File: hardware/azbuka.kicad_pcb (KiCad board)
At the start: 2 copper layers, 10 parts, among them IC1 ATTINY85-S, P1 USB_OTG, P2 CONN_01X06, Q1 MOSFET_P_CH, U1 AP111733, U2 TXS0102, U3 SJ1-3524NG

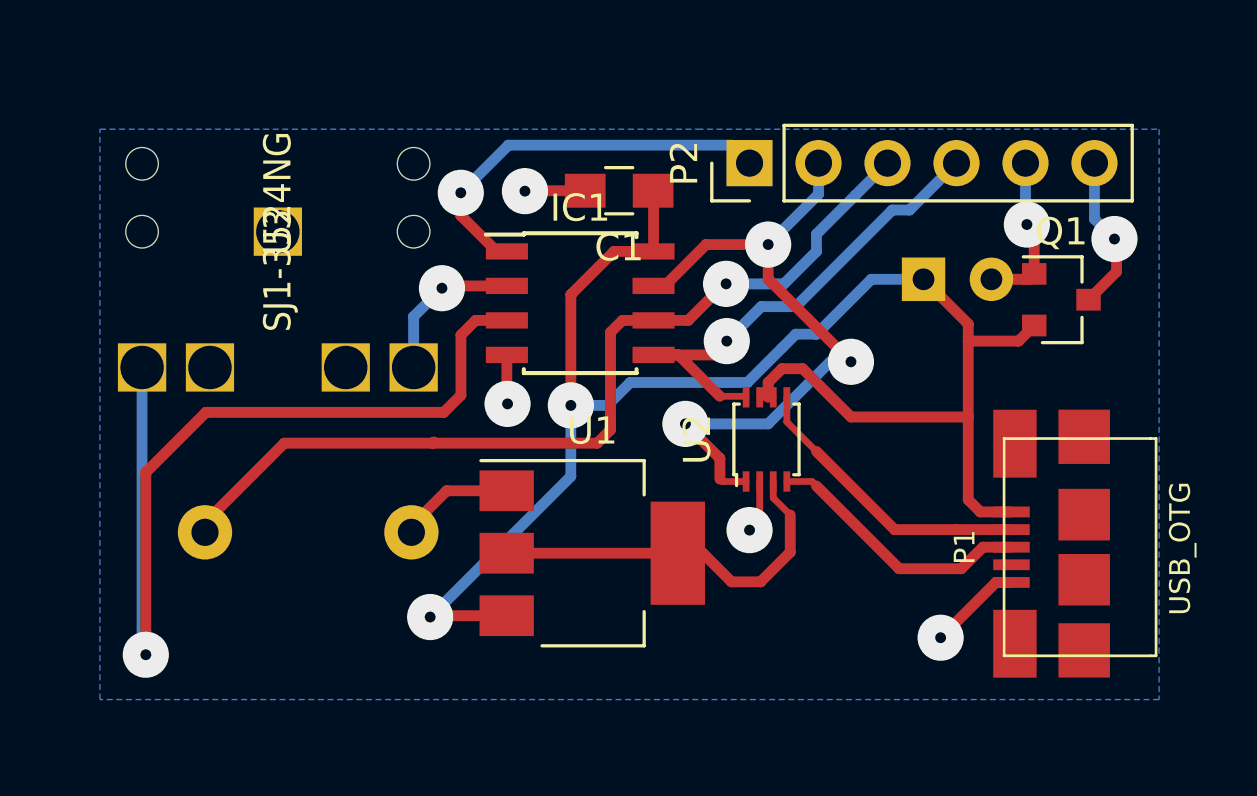
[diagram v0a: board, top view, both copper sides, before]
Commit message: Updating board file to include USB's required series resistors, 1.5k pullup; fixed ATTINY85 footprint; minor layout changes.
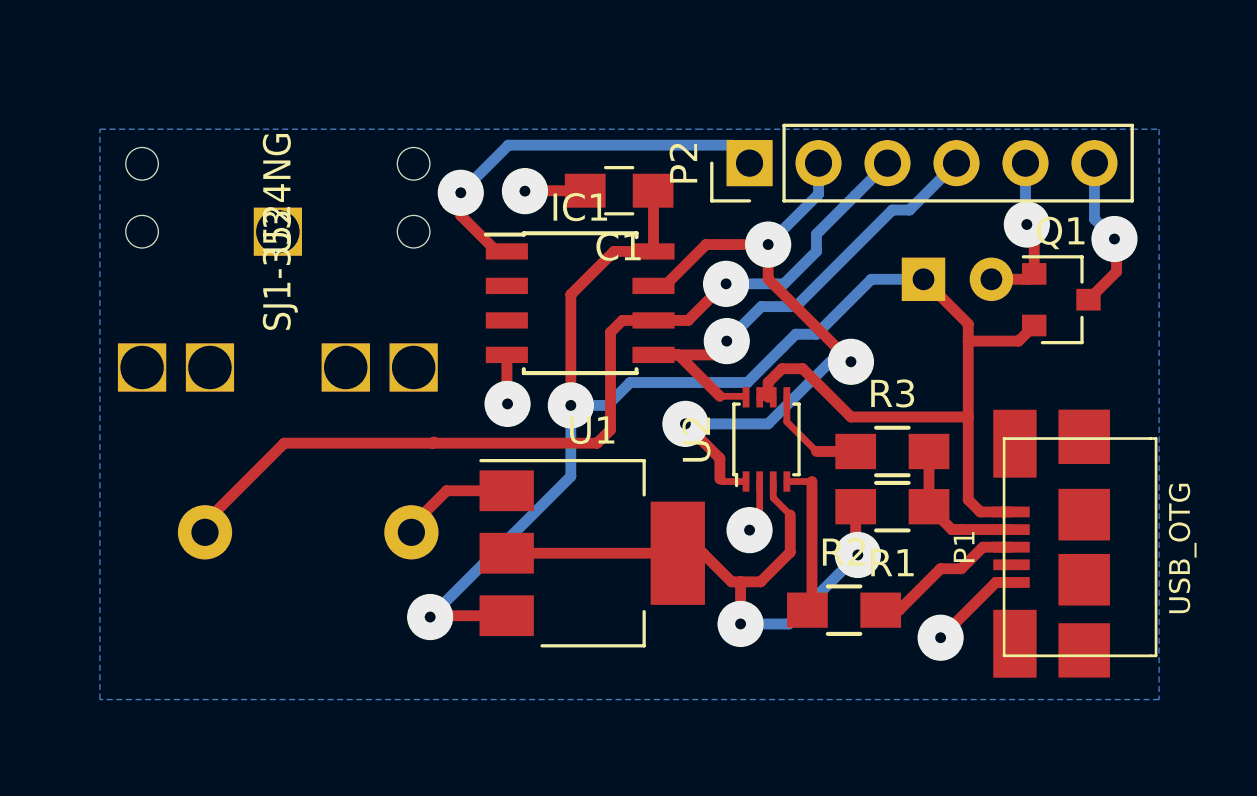
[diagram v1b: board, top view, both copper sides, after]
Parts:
- added R1: 1.5k, Resistors_SMD:R_0805_HandSoldering, F.Cu at (154.2, 72.9)
- added R2: 47, Resistors_SMD:R_0805_HandSoldering, F.Cu at (152.4, 76.7)
- added R3: 47, Resistors_SMD:R_0805_HandSoldering, F.Cu at (154.2, 70.9)
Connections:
- U2 pad 4: Net-(P1-Pad3) -> Net-(R2-Pad1)
- U2 pad 5: Net-(P1-Pad2) -> Net-(R3-Pad1)
- U3 pad 2: DAH -> DIT
- U3 pad 3: DIT -> DAH
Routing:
- net DAH: track 34.3 -> 0.00 mm, vias 1 -> 0
- net +3V3: track 14.2 -> 23.0 mm, vias 0 -> 2
- net DIT: track 5.78 -> 0.00 mm, vias 1 -> 0
- net Net-(R2-Pad1): track 0.00 -> 5.73 mm
- net Net-(P1-Pad2): track 10.8 -> 5.59 mm
- net Net-(P1-Pad3): track 9.93 -> 5.78 mm
- net Net-(R3-Pad1): track 0.00 -> 3.89 mm

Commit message: Minor alterations.
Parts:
- IC1: footprint azbuka:SOIC-8-1EP_3.9x4.9mm_Pitch1.27mm -> ATTINY85-20SU:SOIC127P798X216-8N
- LS1: moved to F.Cu
- U3: moved to B.Cu
- moved U3 3.87 mm to (128.6, 65.2), turned to 0 degrees
- moved IC1 0.81 mm to (141.9, 65.4)
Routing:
- net DIT: track 0.00 -> 7.72 mm
- net DAH: track 0.00 -> 7.61 mm
- net GND: track 20.2 -> 27.8 mm, vias 5 -> 7
- net (no net): track 0.00 -> 1.81 mm, vias 0 -> 1
- net +5V: track 60.4 -> 62.1 mm, vias 2 -> 3
- net RESET: track 14.7 -> 13.7 mm
- net MISO: track 33.6 -> 33.7 mm, vias 1 -> 2

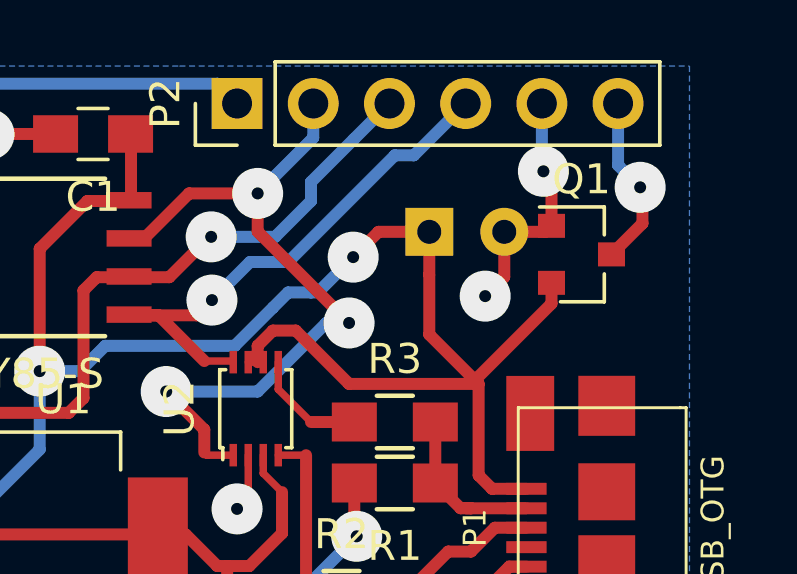
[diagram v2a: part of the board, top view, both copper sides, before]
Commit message: Updating schematics and masks.
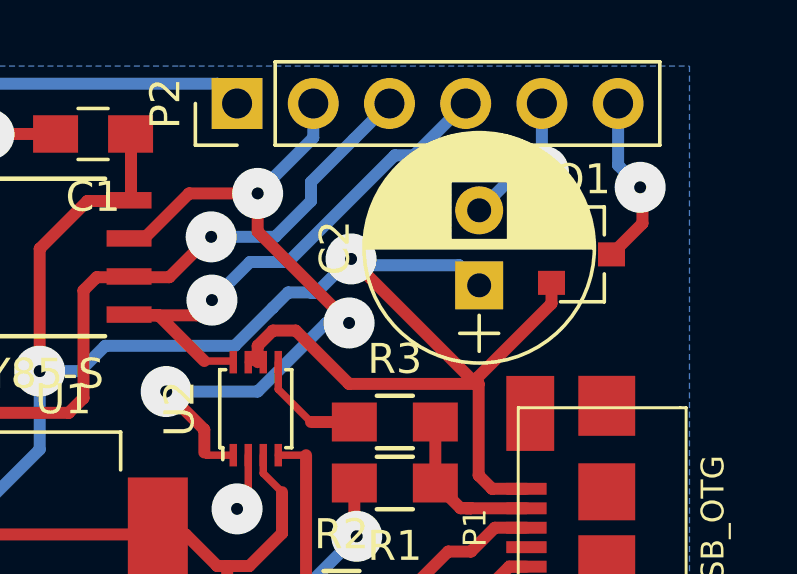
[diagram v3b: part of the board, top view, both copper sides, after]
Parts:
- C2: moved to F.Cu
- moved C2 2.44 mm to (157.0, 66.3), turned to 90 degrees
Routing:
- net +5V: track 62.1 -> 64.5 mm
- net GND: track 27.8 -> 26.7 mm, vias 7 -> 6

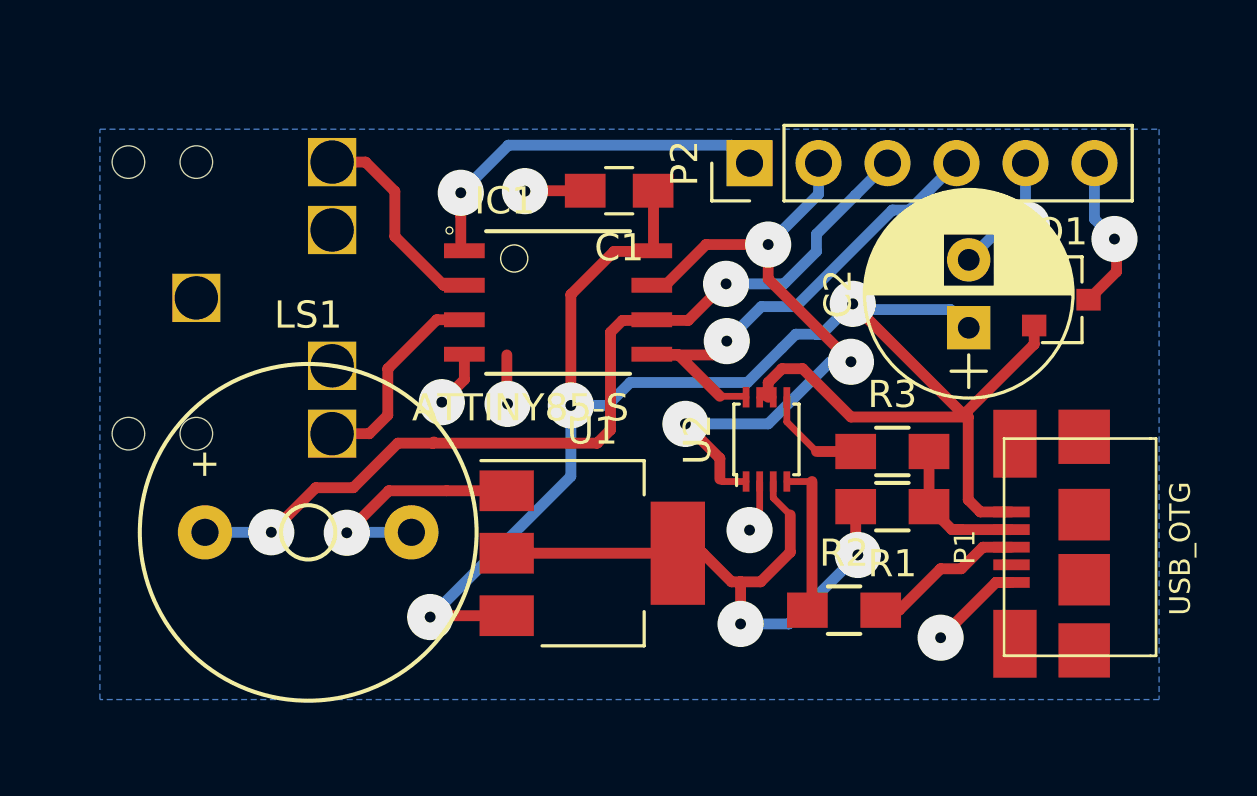
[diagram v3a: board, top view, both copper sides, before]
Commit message: Preparing board version 2.0 (swapping TXB0102 for two 3.6v zeners)
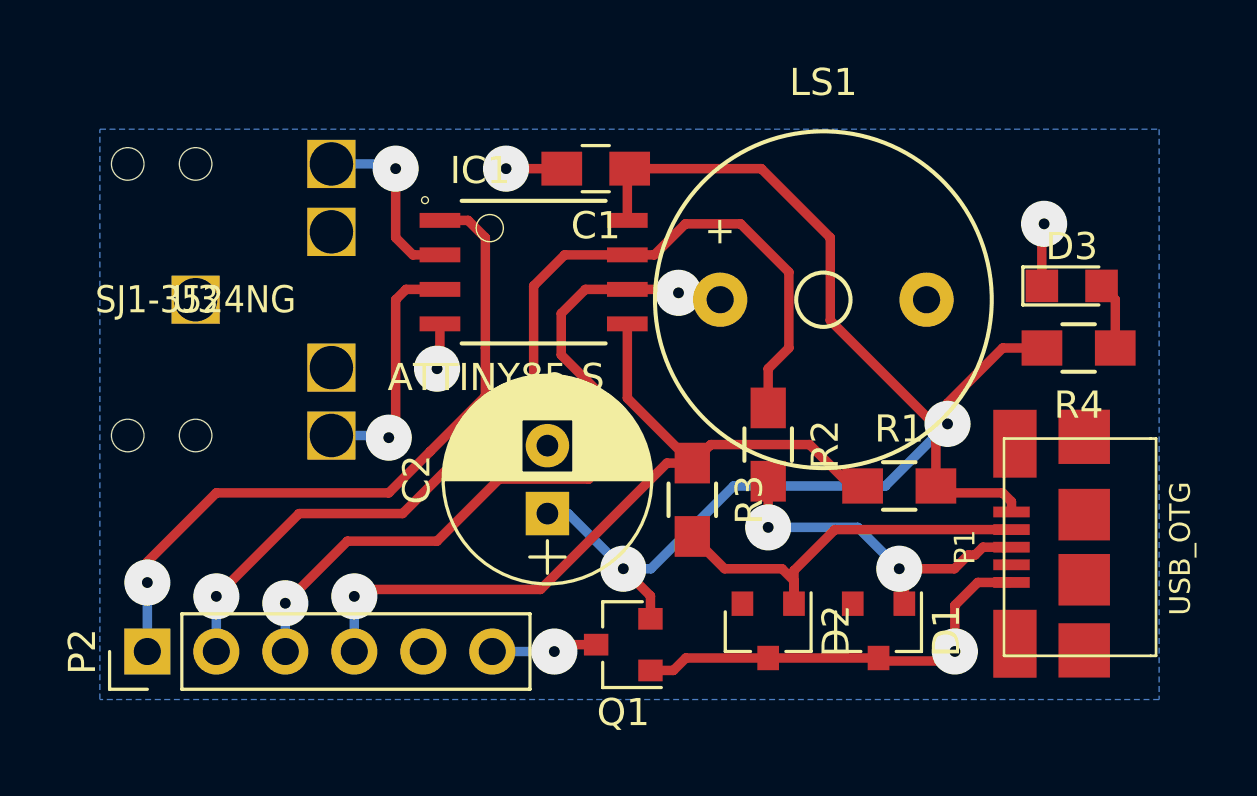
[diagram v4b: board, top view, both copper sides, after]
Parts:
- removed U1: AP111733, TO_SOT_Packages_SMD:SOT-223
- removed U2: TXS0102, Housings_SSOP:VSSOP-8_2.4x2.1mm_Pitch0.5mm
- added D1: 3.6, Diodes_SMD:D_SOT-23_ANK, F.Cu at (153.7, 77.5)
- added D2: 3.6, Diodes_SMD:D_SOT-23_ANK, F.Cu at (149.6, 77.5)
- added D3: LED, LEDs:LED_0805, F.Cu at (160.8, 64.8)
- added R4: R_Small, Resistors_SMD:R_0805_HandSoldering, F.Cu at (161.0, 67.1)
- R1: value 1.5k -> 2.2k
- U3: moved to F.Cu
- moved P2 28.5 mm to (126.7, 78.2)
- moved LS1 20.8 mm to (151.6, 65.3)
- moved Q1 20.5 mm to (144.3, 78.0), turned to 180 degrees
- moved C2 17.0 mm to (141.5, 73.2)
- moved R3 7.58 mm to (146.8, 72.6), turned to 270 degrees
- moved R2 6.71 mm to (149.6, 70.6), turned to 270 degrees
- moved IC1 1.44 mm to (141.0, 64.3)
- moved C1 1.19 mm to (143.3, 60.5)
- moved R1 0.80 mm to (154.4, 72.1), turned to 0 degrees
- moved U3 0.07 mm to (128.5, 65.3)
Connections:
- IC1 pad 2: DIT -> DAH
- IC1 pad 3: DAH -> DIT
- P1 pad 2: Net-(P1-Pad2) -> Net-(D2-Pad2)
- R1 pad 1: Net-(P1-Pad2) -> MOSI
- R1 pad 2: +3V3 -> +5V
- R2 pad 1: Net-(R2-Pad1) -> SCK
- R3 pad 1: Net-(R3-Pad1) -> MOSI
- R3 pad 2: Net-(P1-Pad2) -> Net-(D2-Pad2)
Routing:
- net +3V3: track 23.0 -> 0.00 mm, vias 2 -> 0
- net Net-(D2-Pad2): track 0.00 -> 15.1 mm
- net +5V: track 64.5 -> 50.3 mm, vias 3 -> 2
- net RESET: track 13.7 -> 26.1 mm
- net SCK: track 24.8 -> 36.9 mm, vias 3 -> 1
- net MOSI: track 18.1 -> 29.8 mm
- net Net-(D1-Pad2): track 5.78 -> 13.2 mm, vias 0 -> 2
- net MISO: track 33.7 -> 28.0 mm
- net Net-(R2-Pad1): track 5.73 -> 0.00 mm
- net Net-(P1-Pad2): track 5.59 -> 0.00 mm
- net GND: track 26.7 -> 21.7 mm, vias 6 -> 4
- net Net-(R3-Pad1): track 3.89 -> 0.00 mm
- net Net-(D3-Pad2): track 0.00 -> 2.49 mm
- net Net-(P2-Pad6): track 5.79 -> 3.93 mm
- net (no net): track 1.81 -> 0.00 mm, vias 1 -> 0
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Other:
- net class Default: clearance 0.3 -> 0.25; trace_width 0.4 -> 0.35
- rule trace_clearance: 0.3 -> 0.25

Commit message: Hardware revision 2.1.
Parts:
- moved D2 0.36 mm to (149.9, 77.2), turned to 90 degrees
- moved D1 0.36 mm to (153.4, 77.2), turned to 90 degrees
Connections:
- D1 pad 1: GND -> Net-(D1-Pad1)
- D1 pad 2: Net-(D1-Pad2) -> GND
- D2 pad 1: GND -> Net-(D2-Pad1)
- D2 pad 2: Net-(D2-Pad2) -> GND
- P1 pad 2: Net-(D2-Pad2) -> Net-(D2-Pad1)
- P1 pad 3: Net-(D1-Pad2) -> Net-(D1-Pad1)
- R2 pad 2: Net-(D1-Pad2) -> Net-(D1-Pad1)
- R3 pad 2: Net-(D2-Pad2) -> Net-(D2-Pad1)
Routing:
- net Net-(D2-Pad2): track 15.1 -> 0.00 mm
- net Net-(D2-Pad1): track 0.00 -> 14.0 mm
- net Net-(D1-Pad2): track 13.2 -> 0.00 mm, vias 2 -> 0
- net Net-(D1-Pad1): track 0.00 -> 13.1 mm, vias 0 -> 2
- net +5V: track 50.3 -> 52.8 mm
- net MISO: track 28.0 -> 30.4 mm
- net GND: track 21.7 -> 23.8 mm
- net MOSI: track 29.8 -> 31.3 mm
- net SCK: track 36.9 -> 37.5 mm

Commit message: Version 3 completed.
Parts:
- removed U3: SJ1-3524NG, azbuka:PIN-4_MODIFIED_NO_HOLES
- added SW1: TACT-SWITCH, azbuka:SMD_RED_TACTILE_SWITCH, F.Cu at (130.4, 65.5)
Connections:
- IC1 pad 2: DAH -> Net-(IC1-Pad2)
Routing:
- net GND: track 23.8 -> 46.9 mm
- net DAH: track 6.87 -> 0.00 mm, vias 1 -> 0
- net DIT: track 9.12 -> 13.1 mm, vias 1 -> 0
